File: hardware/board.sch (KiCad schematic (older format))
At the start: 16 parts, among them P1 CONN_4, P2 CONN_6, P3 CONN_6, Q1 BC547, U1 PIC16F628A, U2 7805

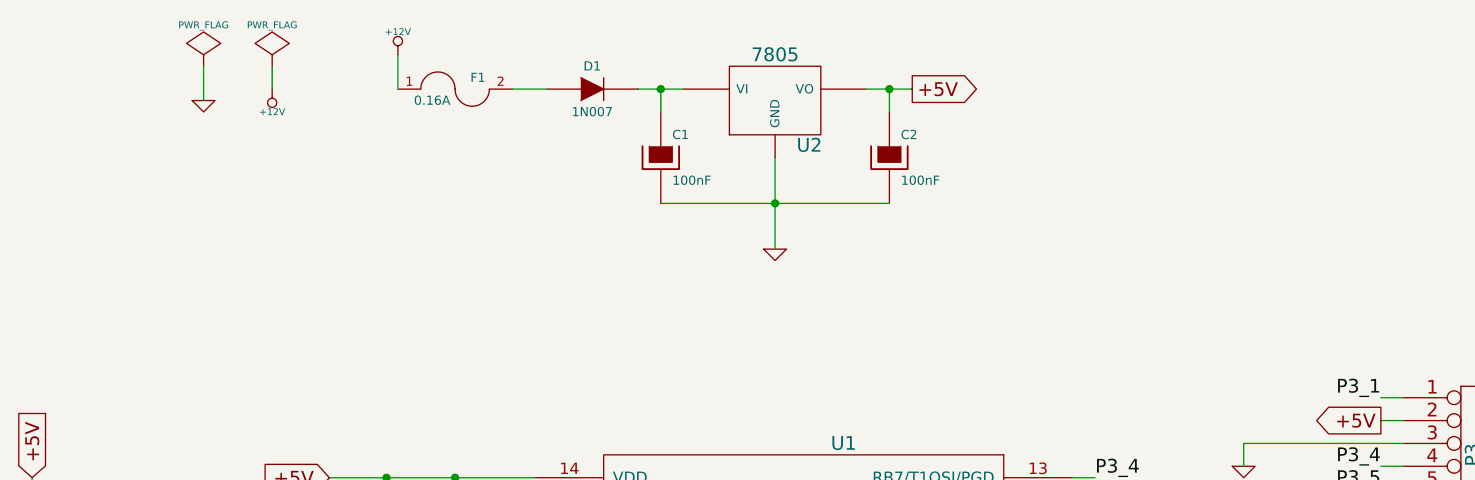
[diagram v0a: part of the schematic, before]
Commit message: Replace LM7805 LVR with LM2576 Buck Converter
Switched to a more efficient power supply plus add a large-ass capacitor
to postpone brownouts during ignition.

closes #1
closes #3
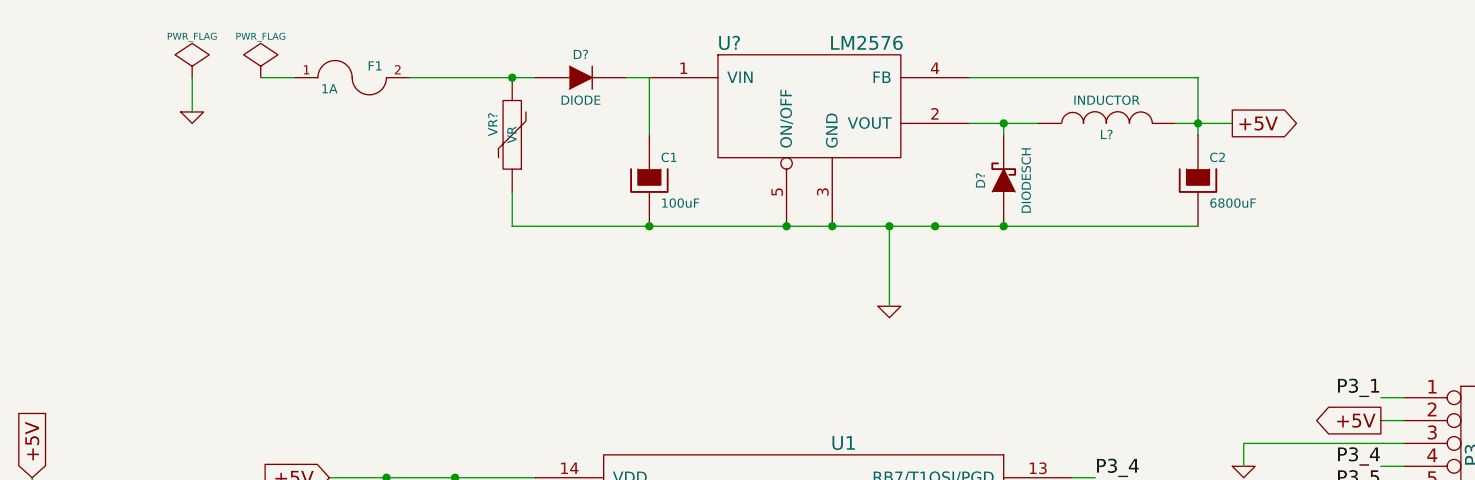
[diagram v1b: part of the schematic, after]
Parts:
- removed D1: 1N007, symbol DIODE
- removed U2: 7805, symbol 7805
- added D?: DIODESCH, symbol DIODESCH
- added D?: DIODE, symbol DIODE
- added L?: INDUCTOR, symbol INDUCTOR
- added U?: LM2576, symbol LM2576
- added VR?: VR, symbol VR
- C1: value 100nF -> 100uF
- C2: value 100nF -> 6800uF
- F1: value 0.16A -> 1A
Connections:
- net +5V: now also L?.2, U?.4 (FB)
- net GND: now also D?.1 (A), U?.3 (GND), U?.5 (ON/OFF), VR?.1
- net at C1.1: now also D?.2 (K), U?.1 (VIN)
- net at F1.2: now also D?.1 (A), VR?.2
- net +12V: no longer names the net of F1.1
- new net: D?.2 (K), L?.1, U?.2 (VOUT)
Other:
- moved on the sheet: C1, C2, F1

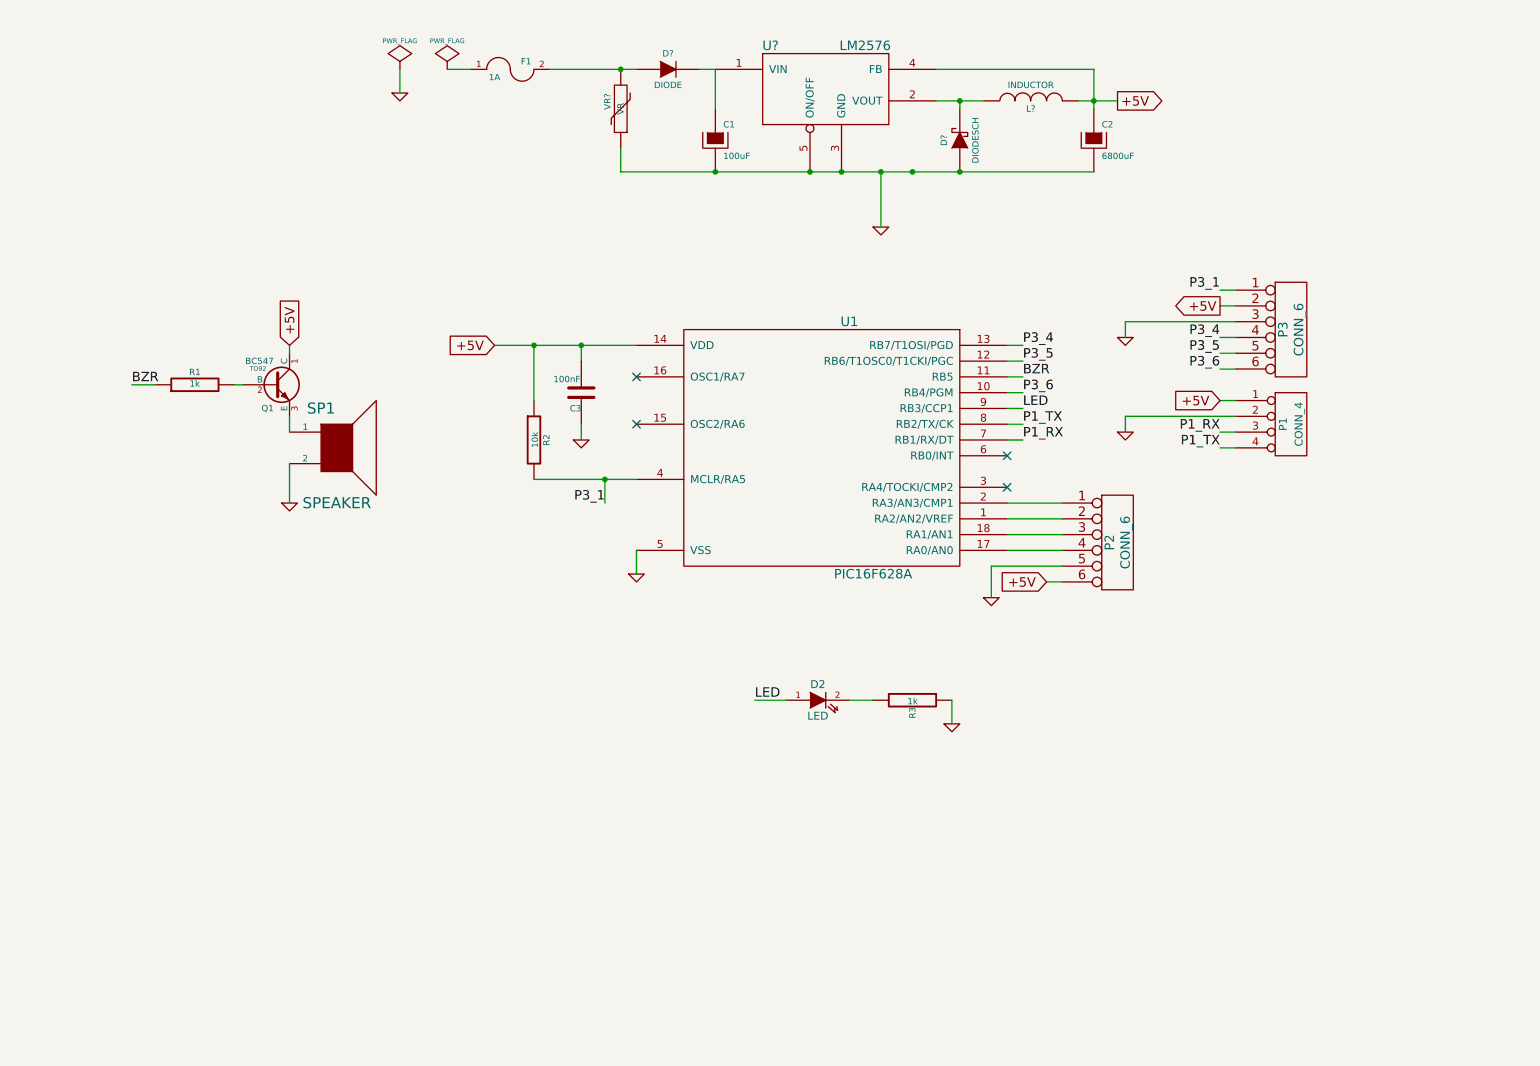
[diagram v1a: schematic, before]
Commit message: Refactor schema to include MOSFET & optocouplers
Use N-channel MOSFETS for "high-side" switching
Add optocouplers to isolate control & bike circuits
10V LVR for bootstrap cap charge/power supply
Purge mislabeled connector (P2 was mislabeled as Pickit 3 conn)
Add screw terminal connectors

(labeling/numbering is still incomplete)
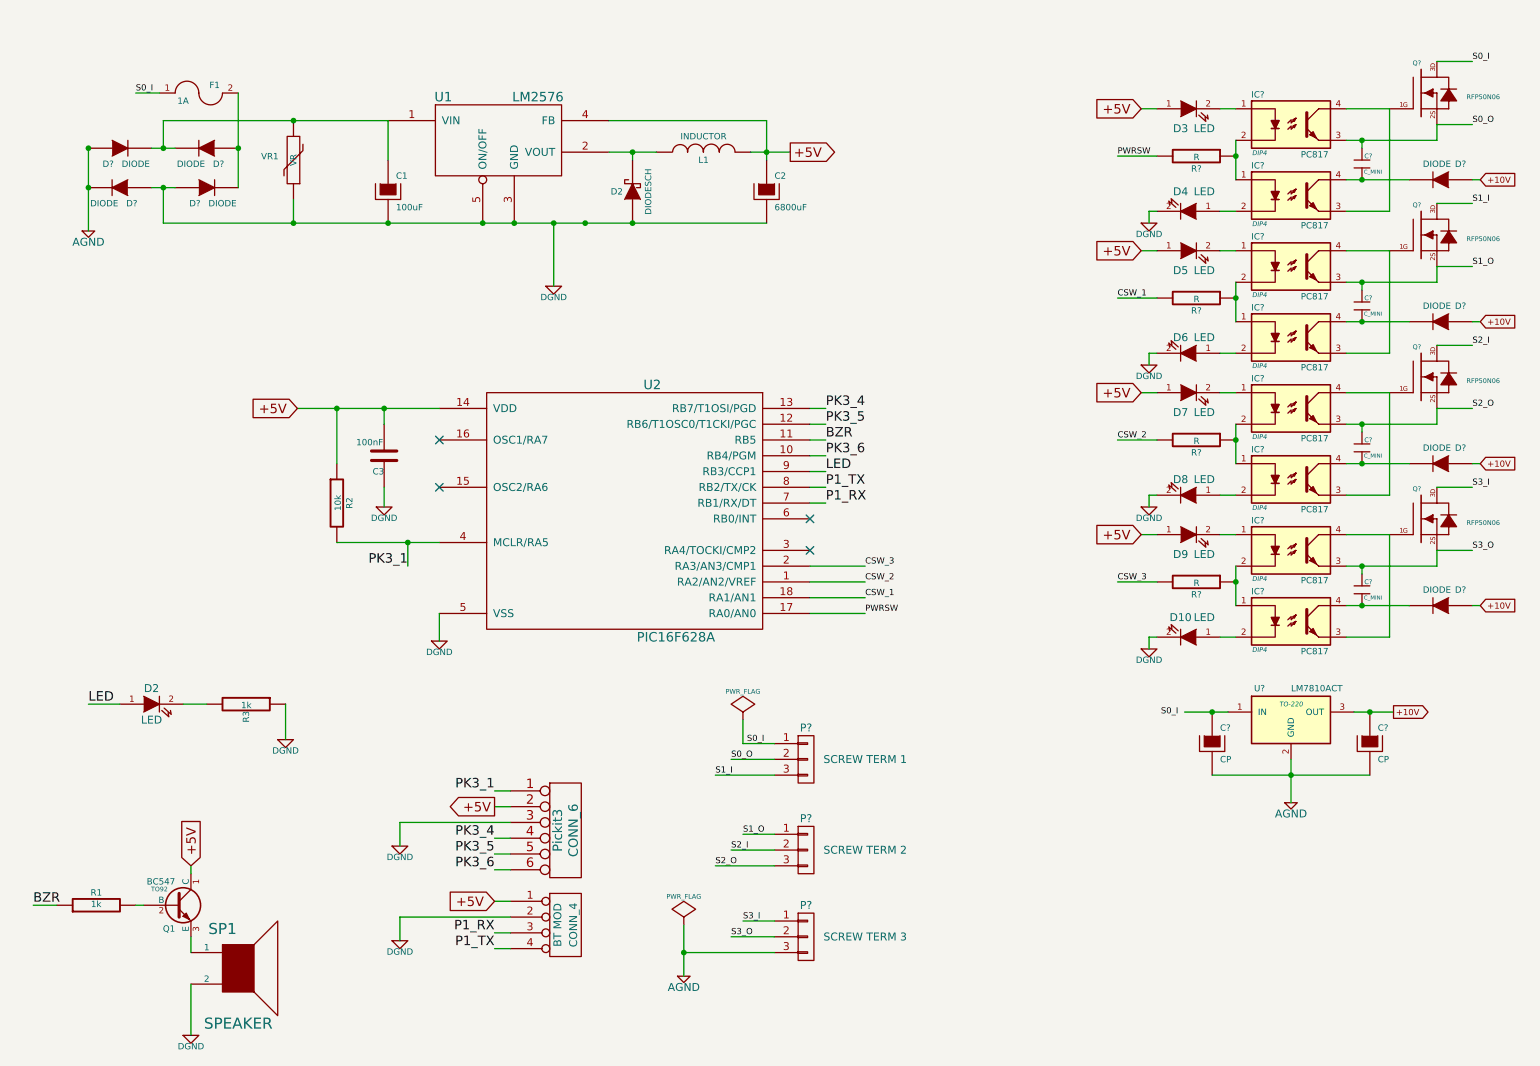
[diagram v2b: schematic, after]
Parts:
- removed D?: DIODE, symbol DIODE
- removed P2: CONN_6, symbol CONN_6
- added C? (x4): C_MINI, symbol C_MINI
- added C? (x2): CP, symbol CP
- added D10, D3, D4, D5, D6, D7, D8, D9: LED, symbol LED
- added D? (x8): DIODE, symbol DIODE
- added IC? (x8): PC817, DIP4, symbol PC817
- added P?: SCREW TERM 1, symbol CONN_01X03
- added P?: SCREW TERM 2, symbol CONN_01X03
- added P?: SCREW TERM 3, symbol CONN_01X03
- added Q? (x4): RFP50N06, symbol MOSFET_N_Opendous
- added R? (x4): R, symbol R
- added U?: LM7810ACT, TO-220, symbol LM7810ACT
- gave numbers to parts that had none: 4
- renumbered P1 to BT, P3 to Pickit3, U1 to U2
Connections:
- net +5V: now also D3.1 (A), D5.1 (A), D7.1 (A), D9.1 (A)
- net CSW_2: now reaches U2.1 (RA2/AN2/VREF)
- net CSW_2: now also R?.2
- net PWRSW: now reaches U2.17 (RA0/AN0)
- net PWRSW: now also R?.2
- net CSW_1: now reaches U2.18 (RA1/AN1)
- net CSW_1: now also R?.2
- net CSW_3: now reaches U2.2 (RA3/AN3/CMP1)
- net CSW_3: now also R?.2
- net S0_I: now reaches F1.1
- net S0_I: now also P?.1 (P1), Q?.3 (D)
- net at F1.2: now also D?.1 (A), D?.2 (K); no longer VR1.2
- net at C1.1, U1.1 (VIN): now also VR1.2, D?.2 (K), D?.2 (K)
- net GND renamed DGND
- net DGND: now also D10.2 (K), D4.2 (K), D6.2 (K), D8.2 (K), D?.1 (A), D?.1 (A)
- net P3_1 renamed PK3_1
- net P3_4 renamed PK3_4
- net P3_5 renamed PK3_5
- net P3_6 renamed PK3_6
- new net: D3.2 (K), IC?.1
- new net: IC?.1, IC?.2, R?.1 (x4)
- new net: IC?.3, IC?.4, Q?.1 (G) (x4)
- new net: D4.1 (A), IC?.2
- new net: C?.2 (B), D?.2 (K), IC?.4 (x4)
- new net: D5.2 (K), IC?.1
- new net: D6.1 (A), IC?.2
- new net: D7.2 (K), IC?.1
- new net: D8.1 (A), IC?.2
- new net: D9.2 (K), IC?.1
- new net: D10.1 (A), IC?.2
- new net: C?.1, U?.1 (IN)
- new net +10V: C?.1, D?.1 (A), D?.1 (A), D?.1 (A), D?.1 (A), U?.3 (OUT)
- new net AGND: C?.2, C?.2, D?.1 (A), D?.2 (K), P?.3 (P3), U?.2 (GND)
- new net S0_O: C?.1 (A), IC?.3, P?.2 (P2), Q?.2 (S)
- new net S1_I: P?.3 (P3), Q?.3 (D)
- new net S1_O: C?.1 (A), IC?.3, P?.1 (P1), Q?.2 (S)
- new net S2_I: P?.2 (P2), Q?.3 (D)
- new net S2_O: C?.1 (A), IC?.3, P?.3 (P3), Q?.2 (S)
- new net S3_I: P?.1 (P1), Q?.3 (D)
- new net S3_O: C?.1 (A), IC?.3, P?.2 (P2), Q?.2 (S)
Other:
- moved on the sheet: BT MOD, C1, C2, C3, D2, F1, L1, Pickit3, Q1, R1, R2, R3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

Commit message: JZ: Label everything + ugly power tag workaround
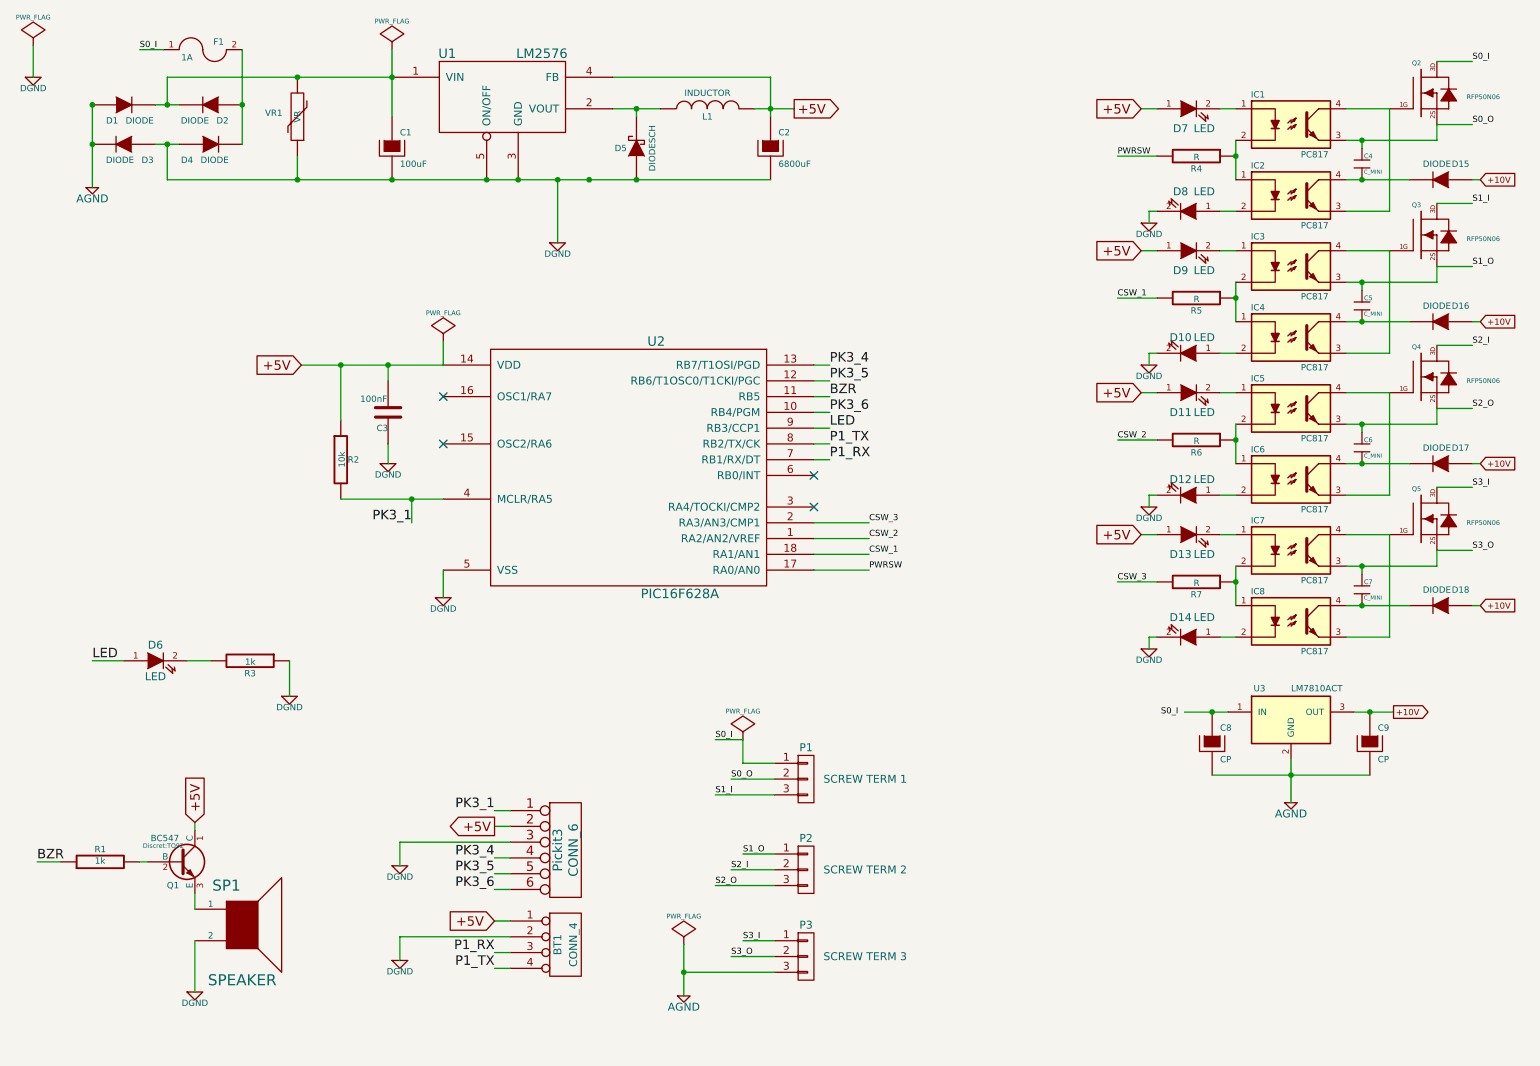
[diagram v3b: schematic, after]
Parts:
- BT1: renamed from BT; footprint (none) -> Connect:SIL-4
- C1: footprint (none) -> Capacitors_ThroughHole:Capacitor10x25RM2.5
- C2: footprint (none) -> Capacitors_ThroughHole:Capacitor16x25RM7.5
- C3: footprint (none) -> Capacitors_ThroughHole:Capacitor7.5MMDiscRM5
- C4, C5, C6, C7: renamed from C?; footprint (none) -> Capacitors_ThroughHole:Capacitor5x11RM2.5
- C8, C9: renamed from C?; footprint (none) -> Capacitors_ThroughHole:Capacitor8x13RM3.8
- D1, D15, D16, D17, D18, D2, D3, D4: renamed from D?; footprint (none) -> Diodes_ThroughHole:Diode_DO-35_SOD27_Horizontal_RM10
- D10: renamed from D6; footprint (none) -> LEDs:LED-5MM
- D11: renamed from D7; footprint (none) -> LEDs:LED-5MM
- D12: renamed from D8; footprint (none) -> LEDs:LED-5MM
- D13: renamed from D9; footprint (none) -> LEDs:LED-5MM
- D14: renamed from D10; footprint (none) -> LEDs:LED-5MM
- D5: renamed from D2; footprint (none) -> Diodes_ThroughHole:Diode_DO-35_SOD27_Horizontal_RM10
- D6: renamed from D2; footprint (none) -> LEDs:LED-5MM
- D7: renamed from D3; footprint (none) -> LEDs:LED-5MM
- D8: renamed from D4; footprint (none) -> LEDs:LED-5MM
- D9: renamed from D5; footprint (none) -> LEDs:LED-5MM
- F1: footprint (none) -> Fuse_Holders_and_Fuses:Fuseholder5x20_horiz_SemiClosed_Casing10x25mm
- IC1, IC2, IC3, IC4, IC5, IC6, IC7, IC8: renamed from IC?; footprint DIP4 -> (none)
- L1: footprint (none) -> Inductors:INDUCTOR_V
- P1, P2, P3: renamed from P?; footprint (none) -> Terminal_Blocks:TerminalBlock_WAGO-236_2Stift_RM5mm_3pol
- Pickit3: footprint (none) -> Connect:SIL-6
- Q1: footprint TO92 -> Discret:TO92
- Q2, Q3, Q4, Q5: renamed from Q?; footprint (none) -> Transistors_TO-220:TO-220_FET-GDS_Vertical_LargePads
- R1, R2, R3: footprint (none) -> Resistors_ThroughHole:Resistor_Vertical_RM5mm
- R4, R5, R6, R7: renamed from R?; footprint (none) -> Resistors_ThroughHole:Resistor_Horizontal_RM20mm
- SP1: footprint (none) -> Buzzers_Beepers:MagneticBuzzer_ProSignal_ABI-009-RC
- U1: footprint (none) -> Sockets_WAGO734:WAGO_734_5pin_Straight_RuggedPads
- U2: footprint (none) -> Sockets_DIP:DIP-18__300_ELL
- U3: renamed from U?; footprint TO-220 -> Transistors_TO-220:TO-220_FET-GDS_Vertical_MountedFromLS_LargePads
- VR1: footprint (none) -> Capacitors_ThroughHole:Capacitor12MMDiscRM7.75
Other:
- moved on the sheet: BT1, C1, C2, C3, D1, D2, D3, D4, D5, D6, F1, L1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

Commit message: Heavily modded pcb + New footprint associations
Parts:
- removed Q2, Q3, Q4, Q5: RFP50N06, Transistors_TO-220:TO-220_FET-GDS_Vertical_LargePads, symbol MOSFET_N_Opendous
- removed U3: LM7810ACT, Transistors_TO-220:TO-220_FET-GDS_Vertical_MountedFromLS_LargePads, symbol LM7810ACT
- added Q2, Q3, Q4, Q5: RFP50N06, Transistors_TO-220:TO-220_FET-GDS_Vertical_LargePads, symbol MOSFET_N
- added U3: LM7810, moje's kicad footprints:78XX, symbol LM7805
- BT1: footprint Connect:SIL-4 -> Pin_Headers:Pin_Header_Straight_1x04
- IC1, IC2, IC3, IC4, IC5, IC6, IC7, IC8: footprint (none) -> opto:DIP-4__300
- P1, P2, P3: footprint Terminal_Blocks:TerminalBlock_WAGO-236_2Stift_RM5mm_3pol -> Connect:bornier3
- Pickit3: footprint Connect:SIL-6 -> Pin_Headers:Pin_Header_Straight_1x06
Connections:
- net +10V: now also U3.VO
- net AGND: now also U3.GND
- net S0_I: now also C8.1, Q2.D, U3.VI
- net S0_O: now also Q2.S
- net S1_I: now also Q3.D
- net S1_O: now also Q3.S
- net S2_I: now also Q4.D
- net S2_O: now also Q4.S
- net S3_I: now also Q5.D
- net S3_O: now also Q5.S
- net at IC1.4, IC2.3: now also Q2.G
- net at IC3.4, IC4.3: now also Q3.G
- net at IC5.4, IC6.3: now also Q4.G
- net at IC7.4, IC8.3: now also Q5.G
